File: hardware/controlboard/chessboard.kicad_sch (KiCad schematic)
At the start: 19 parts, among them J3 Conn_02x04_Counter_Clockwise, U3 AMS1117-3.3

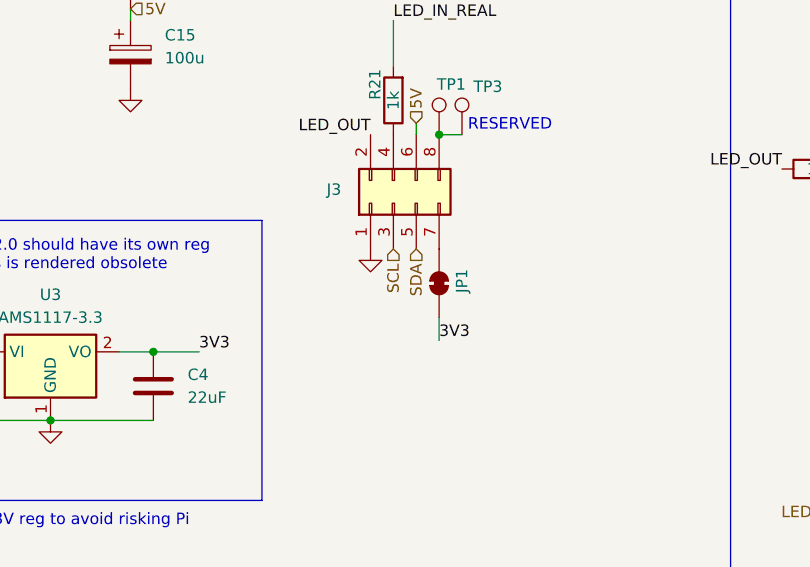
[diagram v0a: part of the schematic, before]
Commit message: Revert controlboard to June 12th 2024
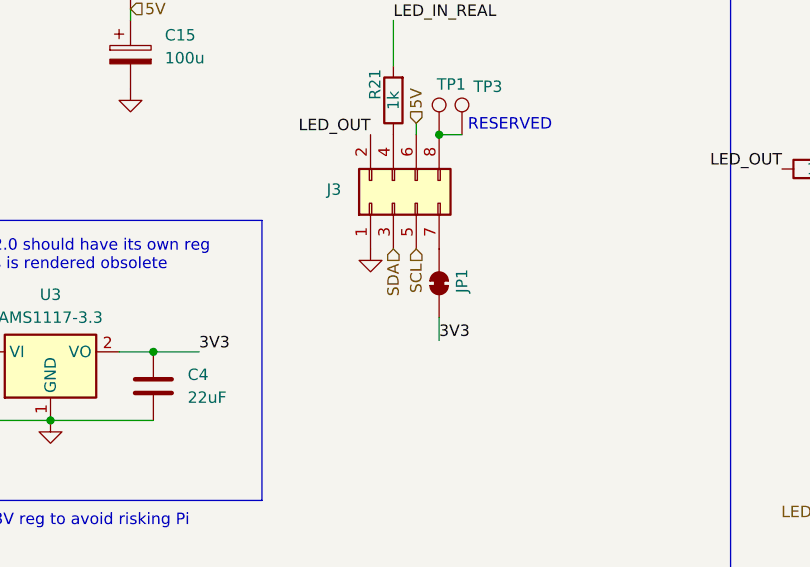
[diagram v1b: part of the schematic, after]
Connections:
- net SCL: now also J3.5 (Pin_5); no longer J3.3 (Pin_3)
- net SDA: now also J3.3 (Pin_3); no longer J3.5 (Pin_5)
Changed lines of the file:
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@@
+		)
+	)
+	(hierarchical_label "SCL"
+		(shape input)
+		(at 171.45 83.82 270)
+		(fields_autoplaced yes)
+		(effects
+			(font
+				(size 1.27 1.27)
+			)
+			(justify right)
 		)
 	)
@@
 		)
 	)
-	(hierarchical_label "SCL"
+	(hierarchical_label "SDA"
 		(shape input)
 		(at 168.91 83.82 270)
@@
 		)
 	)
-	(hierarchical_label "SDA"
-		(shape input)
-		(at 171.45 83.82 270)
-		(fields_autoplaced yes)
-		(effects
-			(font
-				(size 1.27 1.27)
-			)
-			(justify right)
-		)
-	)
